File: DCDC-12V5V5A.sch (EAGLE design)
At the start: 37 parts, among them Q10 NMOSFET, Q9 NMOSFET, U1 LM3150MHX/NOPB

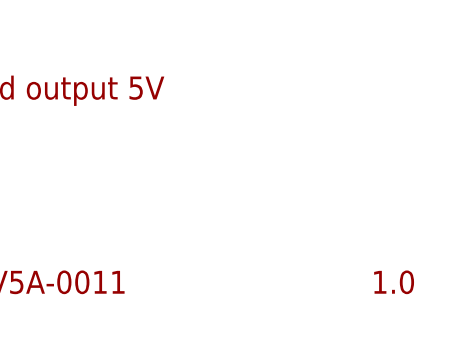
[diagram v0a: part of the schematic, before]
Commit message: Fixed text on schematics. Generated PDF schematics. Removed wrongly committed CSV file.
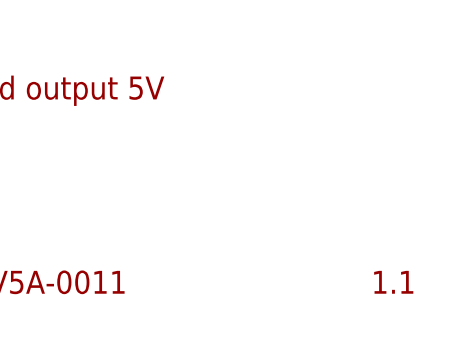
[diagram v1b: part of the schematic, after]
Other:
- note added: "1.1"
- note removed: "1.0"
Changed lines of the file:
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@@
 <sheet>
 <plain>
-<text x="256.54" y="7.62" size="2.54" layer="94">1.0</text>
+<text x="256.54" y="7.62" size="2.54" layer="94">1.1</text>
 <text x="195.58" y="7.62" size="2.54" layer="94">DCDC-12V5V5A-0011</text>
 <text x="165.1" y="25.4" size="2.54" layer="94">DC-DC Buck Converter with fixed output 5V

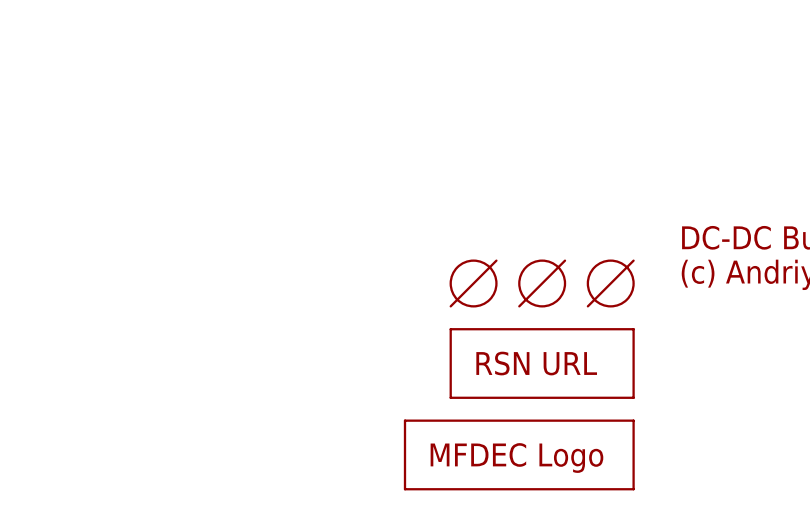
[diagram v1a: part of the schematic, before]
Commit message: Moved some texts and tooling holes a bit. Generated CAM files. Generated PNG preview. Generated PDF schematics. Renamed BoM and PnP files.
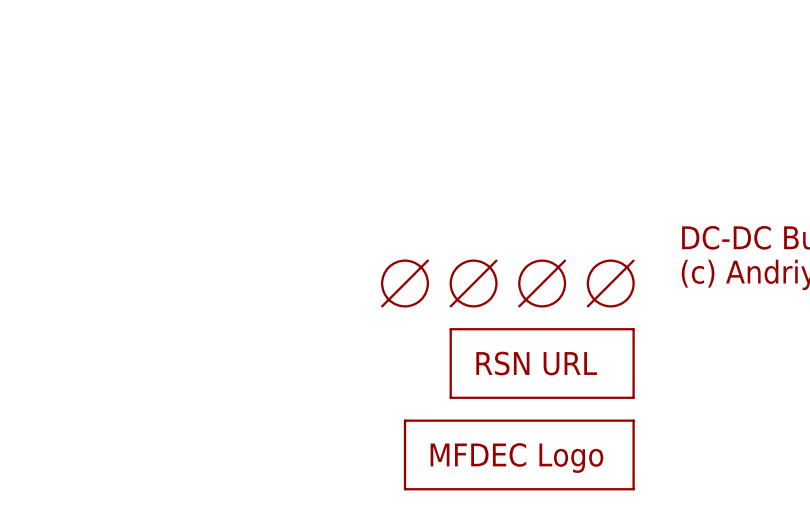
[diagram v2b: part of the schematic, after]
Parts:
- added HOLE4: TOOLINGHOLE, _my_fiducia:TOOLINGHOLE
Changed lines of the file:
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@@
 <part name="SUPPLY4" library="SparkFun-PowerSymbols" library_urn="urn:adsk.eagle:library:530" deviceset="VIN" device=""/>
 <part name="GND1" library="SparkFun-PowerSymbols" library_urn="urn:adsk.eagle:library:530" deviceset="GND" device=""/>
+<part name="HOLE4" library="_my_fiducia" deviceset="TOOLINGHOLE" device=""/>
 </parts>
 <sheets>
@@
 <attribute name="VALUE" x="30.48" y="106.426" size="1.778" layer="96" align="top-center"/>
 </instance>
+<instance part="HOLE4" gate="G$1" x="134.62" y="25.4" smashed="yes"/>
 </instances>
 <busses>

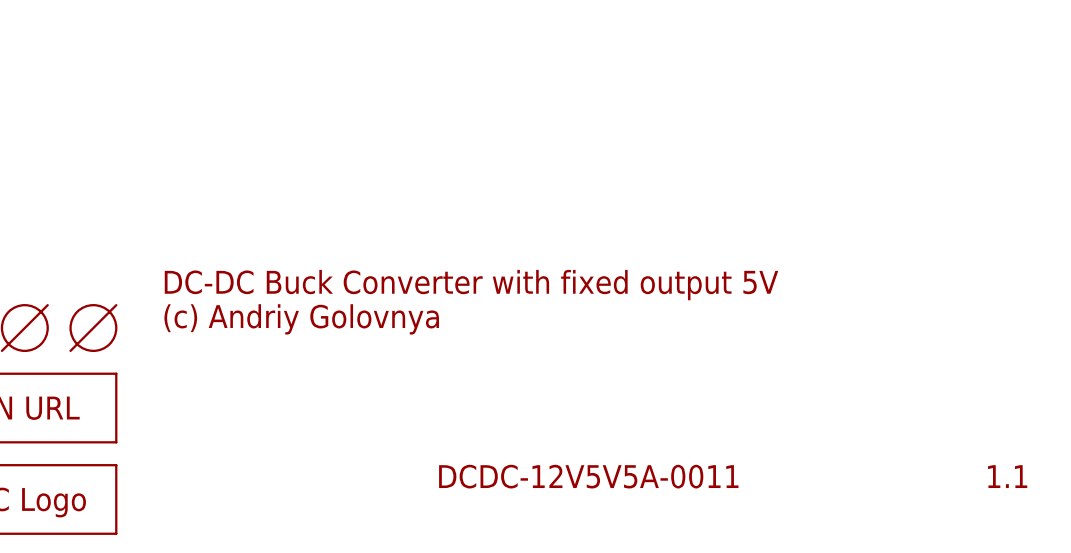
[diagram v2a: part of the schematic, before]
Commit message: Fixed typo. Generated PDF schematics.
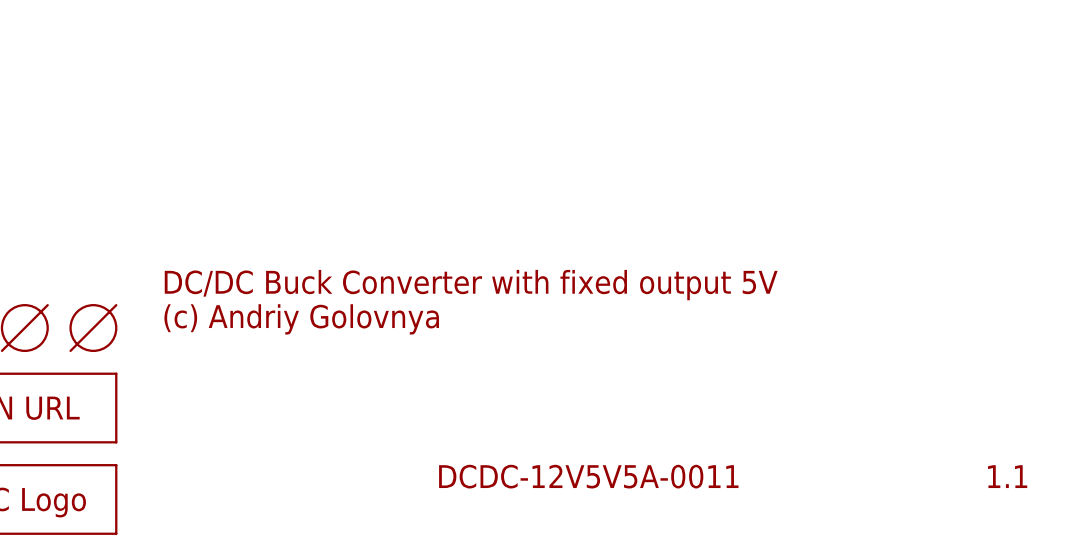
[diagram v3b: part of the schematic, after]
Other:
- note added: "DC/DC Buck Converter with fixed output 5V (c) Andriy Golovnya"
- note removed: "DC-DC Buck Converter with fixed output 5V (c) Andriy Golovnya"
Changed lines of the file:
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@@
 <text x="256.54" y="7.62" size="2.54" layer="94">1.1</text>
 <text x="195.58" y="7.62" size="2.54" layer="94">DCDC-12V5V5A-0011</text>
-<text x="165.1" y="25.4" size="2.54" layer="94">DC-DC Buck Converter with fixed output 5V
+<text x="165.1" y="25.4" size="2.54" layer="94">DC/DC Buck Converter with fixed output 5V
 (c) Andriy Golovnya</text>
 <text x="106.68" y="137.16" size="2.54" layer="94">12V to 5V Conversion</text>
